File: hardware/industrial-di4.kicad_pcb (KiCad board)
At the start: 2 copper layers, 40 x 40 mm, 33 parts, among them P1 CON-SENSOR2, P2 DEBUG, P3 BOOT, P4 Digital Input, U1 XMC1XXX24, U2 LTV846S, U3 DRILL, U4 DRILL, U5 DRILL, U6 DRILL

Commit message: change led position
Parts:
- added Fiducial_Mark: VAL**, kicad-libraries:Fiducial_Mark, F.Cu at (136.3, 71.5)
- moved D5 32.1 mm to (131.1, 40.5), turned to 270 degrees
- moved D4 30.2 mm to (129.5, 40.5), turned to 270 degrees
- moved G*** 29.5 mm to (101.3, 53.5)
- moved D3 28.2 mm to (127.9, 40.5), turned to 270 degrees
- moved D2 26.3 mm to (126.3, 40.5), turned to 270 degrees
- moved RP2 21.2 mm to (124.7, 45.5)
- moved RP3 12.4 mm to (130.1, 48.4), turned to 90 degrees
- moved P2 8.81 mm to (99.8, 44.5)
- moved P3 8.68 mm to (100.6, 49.0), turned to 90 degrees
- moved C3 6.17 mm to (116.6, 44.6), turned to 180 degrees
- moved C2 5.78 mm to (105.8, 38.9)
- moved RP1 5.60 mm to (105.6, 41.0), turned to 0 degrees
- moved C4 4.75 mm to (103.6, 49.5), turned to 180 degrees
- moved C1 2.69 mm to (119.8, 44.5)
- moved R1 2.47 mm to (107.9, 40.5), turned to 90 degrees
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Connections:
- RP1 pad 1: Net-(P1-Pad4) -> S-CS
- RP1 pad 2: Net-(P1-Pad5) -> S-CLK
- RP1 pad 3: Net-(P1-Pad6) -> S-MOSI
- RP1 pad 4: Net-(C2-Pad1) -> S-MISO
- RP1 pad 5: S-MISO -> Net-(C2-Pad1)
- RP1 pad 6: S-MOSI -> Net-(P1-Pad6)
- RP1 pad 7: S-CLK -> Net-(P1-Pad5)
- RP1 pad 8: S-CS -> Net-(P1-Pad4)
- RP2 pad 1: Net-(D2-Pad2) -> LED0
- RP2 pad 2: Net-(D3-Pad2) -> LED1
- RP2 pad 3: Net-(D4-Pad2) -> LED2
- RP2 pad 4: Net-(D5-Pad2) -> LED3
- RP2 pad 5: Net-(RP2-Pad5) -> Net-(D5-Pad2)
- RP2 pad 6: Net-(RP2-Pad6) -> Net-(D4-Pad2)
- RP2 pad 7: Net-(RP2-Pad7) -> Net-(D3-Pad2)
- RP2 pad 8: Net-(RP2-Pad8) -> Net-(D2-Pad2)
- U1 pad 1: S-MISO -> Net-(P2-Pad1)
- U1 pad 13: (no net) -> LED3
- U1 pad 14: (no net) -> LED2
- U1 pad 15: Net-(RP2-Pad8) -> LED1
- U1 pad 16: Net-(RP2-Pad7) -> LED0
- U1 pad 17: Net-(RP2-Pad6) -> S-MISO
- U1 pad 18: Net-(RP2-Pad5) -> S-MOSI
- U1 pad 19: (no net) -> S-CLK
- U1 pad 2: Net-(R1-Pad1) -> (no net)
- U1 pad 20: (no net) -> S-CS
- U1 pad 21: Net-(P2-Pad1) -> Net-(R1-Pad1)
- U1 pad 22: S-CS -> (no net)
- U1 pad 23: S-CLK -> (no net)
- U1 pad 24: S-MOSI -> (no net)
- U1 pad 3: (no net) -> INPUT1
- U1 pad 4: (no net) -> INPUT2
- U1 pad 5: (no net) -> INPUT3
- U1 pad 6: (no net) -> INPUT4
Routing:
- net INPUT3: track 2.51 -> 33.6 mm, vias 0 -> 2
- net INPUT2: track 4.97 -> 34.5 mm, vias 0 -> 2
- net INPUT4: track 6.74 -> 32.7 mm, vias 0 -> 2
- net INPUT1: track 9.03 -> 33.9 mm, vias 0 -> 2
- net LED2: track 0.00 -> 19.6 mm
- net LED0: track 0.00 -> 19.2 mm
- net LED1: track 0.00 -> 18.7 mm
- net LED3: track 0.00 -> 18.5 mm
- net Net-(P1-Pad5): track 7.10 -> 15.4 mm, vias 0 -> 2
- net Net-(P1-Pad4): track 8.64 -> 16.6 mm, vias 0 -> 2
- net Net-(P1-Pad6): track 5.67 -> 13.6 mm, vias 0 -> 2
- net Net-(C2-Pad1): track 5.58 -> 13.4 mm, vias 0 -> 2
- net Net-(D5-Pad2): track 1.61 -> 8.54 mm
- net Net-(RP2-Pad5): track 5.69 -> 0.00 mm
- net Net-(D4-Pad2): track 1.40 -> 7.02 mm
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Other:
- net class Default: via_dia 0.70104 -> 0.7; via_drill 0.24892 -> 0.25
- rule via_min_drill: 0.24892 -> 0.25
- rule via_min_size: 0.70104 -> 0.55

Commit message: add missing text informations
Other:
- board text added: "Copyright Tinkerforge GmbH 2017. This documentation describes Open Hardware and is licensed under the CERN OHL v. 1.1. You may redistribute and modify this documentation under the terms of the CERN OHL v.1.1. (http://ohwr.org/cernohl). This documentation is distributed WITHOUT ANY EXPRESS OR IMPLIED WARRANTY, INCLUDING OF MERCHANTABILITY, SATISFACTORY QUALITY AND FITNESS FOR A PARTICULAR PURPOSE.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"
- board text removed: "Copyright Tinkerforge GmbH 2012. This documentation describes Open Hardware and is licensed under the CERN OHL v. 1.1. You may redistribute and modify this documentation under the terms of the CERN OHL v.1.1. (http://ohwr.org/cernohl). This documentation is distributed WITHOUT ANY EXPRESS OR IMPLIED WARRANTY, INCLUDING OF MERCHANTABILITY, SATISFACTORY QUALITY AND FITNESS FOR A PARTICULAR PURPOSE.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"
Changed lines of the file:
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@@
     (links 73)
     (no_connects 0)
-    (area 97.609659 37.858699 137.993121 78.242161)
+    (area 96.944659 37.196239 281.59583 171.39285)
     (thickness 1.6002)
     (drawings 34)
@@
   (page A4)
   (title_block
-    (date "21 jan 2013")
+    (title "Industrial Digital In 4 2.0")
+    (date 2017-12-08)
+    (rev 2.0)
+    (company "Tinkerforge GmbH")
+    (comment 1 "Licensed under CERN OHL v.1.1")
+    (comment 2 "Copyright (©) 2017, B.Nordmeyer <bastian@tinkerforge.com>")
   )
   (layers
@@
     (effects (font (size 0.8001 0.8001) (thickness 0.14986)))
   )
-  (gr_text "Copyright Tinkerforge GmbH 2012.\nThis documentation describes Open Hardware and is licensed under the\nCERN OHL v. 1.1.\nYou may redistribute and modify this documentation under the terms of the\nCERN OHL v.1.1. (http://ohwr.org/cernohl). This documentation is distributed\nWITHOUT ANY EXPRESS OR IMPLIED WARRANTY, INCLUDING OF\nMERCHANTABILITY, SATISFACTORY QUALITY AND FITNESS FOR A\nPARTICULAR PURPOSE. Please see the CERN OHL v.1.1 for applicable\nconditions" (at 257.64998 165.0492) (layer Cmts.User)
-    (effects (font (size 0.8001 0.8001) (thickness 0.20066)))
+  (gr_text "Copyright Tinkerforge GmbH 2017.\nThis documentation describes Open Hardware and is licensed under the\nCERN OHL v. 1.1.\nYou may redistribute and modify this documentation under the terms of the\nCERN OHL v.1.1. (http://ohwr.org/cernohl). This documentation is distributed\nWITHOUT ANY EXPRESS OR IMPLIED WARRANTY, INCLUDING OF\nMERCHANTABILITY, SATISFACTORY QUALITY AND FITNESS FOR A\nPARTICULAR PURPOSE. Please see the CERN OHL v.1.1 for applicable\nconditions" (at 259.3 157.05) (layer Cmts.User)
+    (effects (font (size 0.8001 0.8001) (thickness 0.200025)))
   )
   (gr_text "Input\nmax 36V" (at 100.4 68.95 90) (layer F.SilkS)

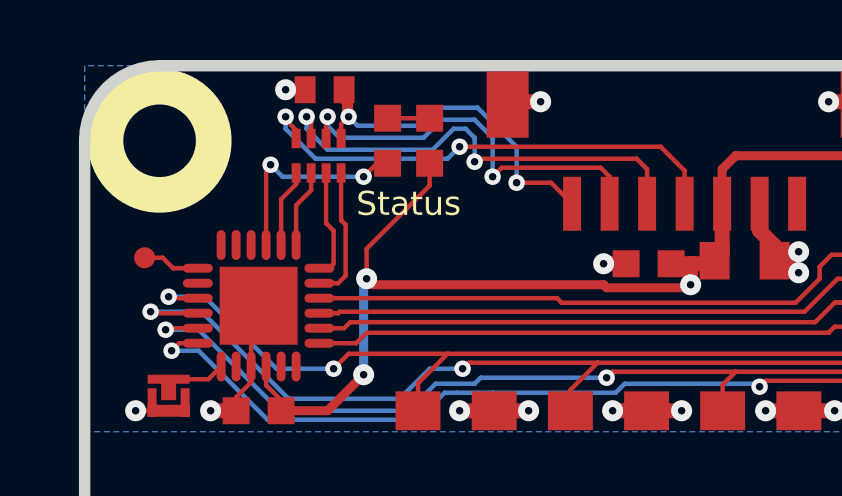
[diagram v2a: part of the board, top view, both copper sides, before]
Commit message: fix spi slave interface pins
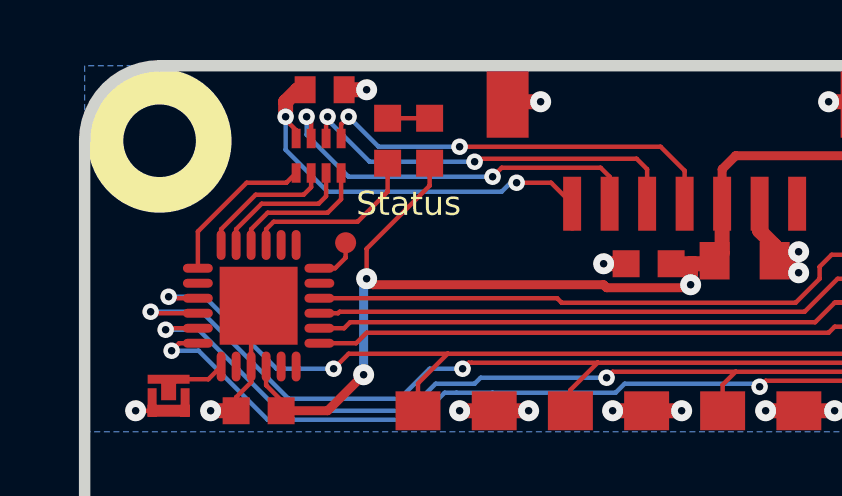
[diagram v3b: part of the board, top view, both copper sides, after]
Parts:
- moved P2 6.72 mm to (106.5, 44.0)
- turned C2 to 0 degrees
- turned RP1 to 180 degrees
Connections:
- RP1 pad 1: S-CS -> Net-(P1-Pad4)
- RP1 pad 2: S-CLK -> Net-(P1-Pad5)
- RP1 pad 3: S-MOSI -> Net-(P1-Pad6)
- RP1 pad 4: S-MISO -> Net-(C2-Pad1)
- RP1 pad 5: Net-(C2-Pad1) -> S-MISO
- RP1 pad 6: Net-(P1-Pad6) -> S-MOSI
- RP1 pad 7: Net-(P1-Pad5) -> S-CLK
- RP1 pad 8: Net-(P1-Pad4) -> S-CS
- U1 pad 1: Net-(P2-Pad1) -> S-MISO
- U1 pad 17: S-MISO -> (no net)
- U1 pad 18: S-MOSI -> Net-(P2-Pad1)
- U1 pad 19: S-CLK -> (no net)
- U1 pad 20: S-CS -> (no net)
- U1 pad 22: (no net) -> S-CS
- U1 pad 23: (no net) -> S-CLK
- U1 pad 24: (no net) -> S-MOSI
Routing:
- net Net-(P1-Pad4): track 16.6 -> 14.1 mm
- net S-CS: track 2.61 -> 4.81 mm
- net S-CLK: track 2.61 -> 4.76 mm
- net Net-(P1-Pad5): track 15.4 -> 13.4 mm
- net Net-(C2-Pad1): track 13.4 -> 14.6 mm
- net S-MOSI: track 3.67 -> 4.58 mm
- net S-MISO: track 4.47 -> 5.31 mm
- net Net-(R1-Pad1): track 6.99 -> 6.39 mm, vias 2 -> 0
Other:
- board text added: "Copyright Tinkerforge GmbH 2018. This documentation describes Open Hardware and is licensed under the CERN OHL v. 1.1. You may redistribute and modify this documentation under the terms of the CERN OHL v.1.1. (http://ohwr.org/cernohl). This documentation is distributed WITHOUT ANY EXPRESS OR IMPLIED WARRANTY, INCLUDING OF MERCHANTABILITY, SATISFACTORY QUALITY AND FITNESS FOR A PARTICULAR PURPOSE.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"
- board text removed: "Copyright Tinkerforge GmbH 2017. This documentation describes Open Hardware and is licensed under the CERN OHL v. 1.1. You may redistribute and modify this documentation under the terms of the CERN OHL v.1.1. (http://ohwr.org/cernohl). This documentation is distributed WITHOUT ANY EXPRESS OR IMPLIED WARRANTY, INCLUDING OF MERCHANTABILITY, SATISFACTORY QUALITY AND FITNESS FOR A PARTICULAR PURPOSE.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"

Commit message: change weee symbol position
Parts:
- moved VAL 1.00 mm to (125.8, 58.0), turned to 270 degrees
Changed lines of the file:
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@@
   (layers
     (0 Front signal)
-    (31 Back signal)
+    (31 Back signal hide)
     (32 B.Adhes user)
     (33 F.Adhes user)
@@
   )
   (module kicad-libraries:WEEE_7mm (layer Back)
-    (at 124.8 58.05 90)
-    (fp_text reference VAL (at 0 0 90) (layer B.SilkS) hide
+    (at 125.8 58.05 270)
+    (fp_text reference VAL (at 0 0 270) (layer B.SilkS) hide
       (effects (font (size 0.2 0.2) (thickness 0.05)) (justify mirror))
     )
-    (fp_text value WEEE_7mm (at 0.75 0 90) (layer B.SilkS) hide
+    (fp_text value WEEE_7mm (at 0.75 0 270) (layer B.SilkS) hide
       (effects (font (size 0.2 0.2) (thickness 0.05)) (justify mirror))
     )

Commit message: fix logo positions
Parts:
- moved G*** 10.0 mm to (127.8, 58.0), turned to 90 degrees
- moved VAL 8.00 mm to (117.8, 58.0), turned to 90 degrees
- moved VAL 2.00 mm to (107.8, 58.0), turned to 90 degrees
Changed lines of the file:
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@@
   )
   (module kicad-libraries:WEEE_7mm (layer Back)
-    (at 125.8 58.05 270)
-    (fp_text reference VAL (at 0 0 270) (layer B.SilkS) hide
+    (at 117.8 58.05 90)
+    (fp_text reference VAL (at 0 0 90) (layer B.SilkS) hide
       (effects (font (size 0.2 0.2) (thickness 0.05)) (justify mirror))
     )
-    (fp_text value WEEE_7mm (at 0.75 0 270) (layer B.SilkS) hide
+    (fp_text value WEEE_7mm (at 0.75 0 90) (layer B.SilkS) hide
       (effects (font (size 0.2 0.2) (thickness 0.05)) (justify mirror))
     )
@@
   )
   (module kicad-libraries:CE_5mm (layer Back)
-    (at 109.8 58.05 270)
-    (fp_text reference VAL (at 0 0 270) (layer B.SilkS) hide
+    (at 107.8 58.05 90)
+    (fp_text reference VAL (at 0 0 90) (layer B.SilkS) hide
       (effects (font (size 0.2 0.2) (thickness 0.05)) (justify mirror))
     )
-    (fp_text value CE_5mm (at 0 0 270) (layer B.SilkS) hide
+    (fp_text value CE_5mm (at 0 0 90) (layer B.SilkS) hide
       (effects (font (size 0.2 0.2) (thickness 0.05)) (justify mirror))
     )
@@
   )
   (module kicad-libraries:Logo_CoMCU (layer Back)
-    (at 117.8 58.05 270)
-    (fp_text reference G*** (at 0 0 270) (layer B.SilkS) hide
+    (at 127.8 58.05 90)
+    (fp_text reference G*** (at 0 0 90) (layer B.SilkS) hide
       (effects (font (thickness 0.3)) (justify mirror))
     )
-    (fp_text value LOGO (at 0.75 0 270) (layer B.SilkS) hide
+    (fp_text value LOGO (at 0.75 0 90) (layer B.SilkS) hide
       (effects (font (thickness 0.3)) (justify mirror))
     )
